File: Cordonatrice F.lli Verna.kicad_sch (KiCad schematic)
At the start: 36 parts, among them J1 Screw_Terminal_3_P5.00mm, J10 Screw_Terminal_2_P5.00mm, J11 Screw_Terminal_2_P5.00mm, J12 Screw_Terminal_4_P5.00mm, J13 Screw_Terminal_2_P5.00mm, J14 Screw_Terminal_2_P5.00mm, J2 Screw_Terminal_3_P5.00mm, J3 Screw_Terminal_3_P5.00mm, J4 Screw_Terminal_3_P5.00mm, J5 Screw_Terminal_3_P5.00mm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

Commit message: sostituzione esp32
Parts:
- removed U1: ESP32-DEVKITC-32UE, ESP32-DEVKITC-32UE:ESPRESSIF_ESP32-DEVKITC-32UE, symbol ESP32-DEVKITC-32UE:ESP32-DEVKITC-32UE
- added U3: ESP32-DEVKITC-32D, ESP32-DEVKITC-32D:MODULE_ESP32-DEVKITC-32D, symbol ESP32-DEVKITC-32D:ESP32-DEVKITC-32D
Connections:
- net +24V: no longer K1.1
- net +3.3V: now also U3.J2-1 (3V3)
- net +5V: now also K1.1, U3.J2-19 (EXT_5V)
- net SCL: now also U3.J3-3 (IO22)
- net SDA: now also U3.J3-6 (IO21)
- net rele_fiaccola: now reaches R1.1
- net rele_fiaccola: now also U3.J3-5 (RXD0)

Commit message: correzione schema corretto
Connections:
- net BT_PAUSE: now also U3.J3-10 (IO5)
- net BT_START: now also U3.J2-13 (IO12)
- net BT_STOP: now also U3.J2-15 (IO13)
- net GND: now also U3.J3-1 (GND3)
- net LIMIT_X_MAX: now also U3.J2-6 (IO35)
- net LIMIT_X_MIN: now also U3.J2-5 (IO34)
- net LIMIT_Y_MAX: now also U3.J2-4 (SENSOR_VN)
- net LIMIT_Y_MIN: now also U3.J2-3 (SENSOR_VP)
- net POT_M1: now also U3.J3-16 (IO15)
- net POT_M2: now also U3.J3-13 (IO4)
- net ENBL_X_MIC.: now reaches U3.J2-10 (IO26)
- net ENBL_X_MIC.: now also U2.3 (A3)
- net DIR_X_MIC.: now reaches U3.J2-11 (IO27)
- net DIR_X_MIC.: now also U2.2 (A2)
- net STEP_X_MIC.: now reaches U3.J2-12 (IO14)
- net STEP_X_MIC.: now also U2.1 (A1)
- net ENBL_Y_MIC.: now reaches U3.J2-7 (IO32)
- net ENBL_Y_MIC.: now also U2.6 (A6)
- net DIR_Y_MIC.: now reaches U3.J2-8 (IO33)
- net DIR_Y_MIC.: now also U2.5 (A5)
- net STEP_Y_MIC.: now reaches U3.J2-9 (IO25)
- net STEP_Y_MIC.: now also U2.4 (A4)
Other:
- moved on the sheet: J14, K1, Q1, R1

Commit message: aggiunta 7824
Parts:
- added C1: 22uF_50V, Capacitor_THT:CP_Radial_D5.0mm_P2.00mm, symbol PCM_SL_Capacitors:22uF_50V
- added C2: 100nF_Ceramic, Capacitor_THT:C_Disc_D5.0mm_W2.5mm_P2.50mm, symbol PCM_SL_Capacitors:100nF_Ceramic
- added U1: LM7812_TO220, Package_TO_SOT_THT:TO-220-3_Vertical, symbol Regulator_Linear:LM7812_TO220
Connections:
- net +24V: now also U1.1 (VI); no longer U4.1 (VI)
- net +5V: now also C1.1, C2.2; no longer C3.2, C6.1
- net GND: now also C1.2, C2.1, U1.2 (GND)
- new net: C3.2, C6.1, U1.3 (VO), U4.1 (VI)
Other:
- moved on the sheet: C3, C4, C5, C6, U4

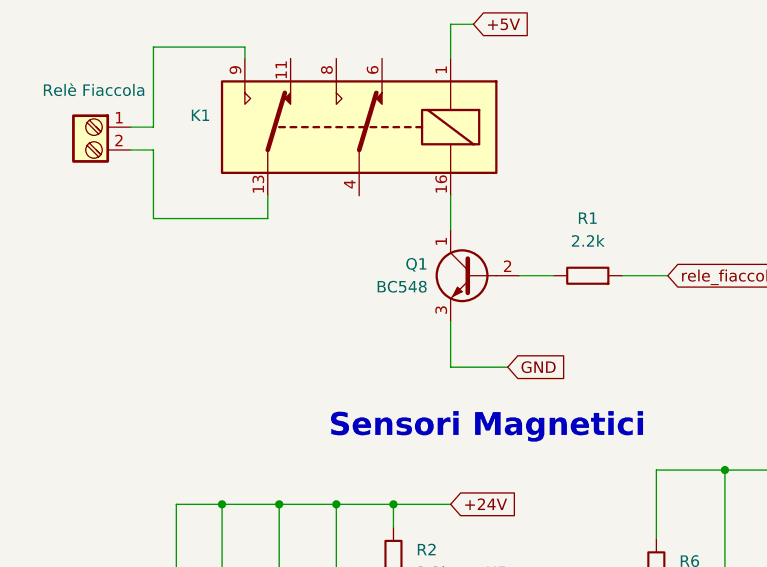
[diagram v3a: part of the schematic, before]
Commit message: aggiunta diodo su transistor
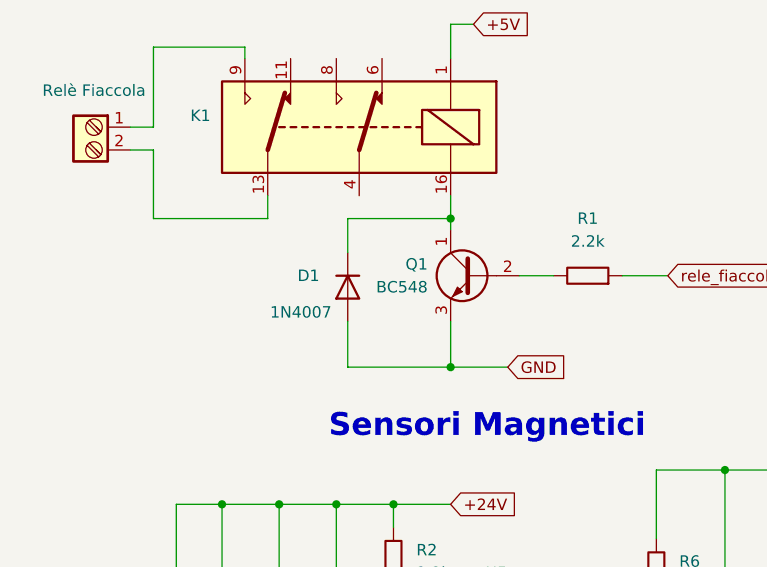
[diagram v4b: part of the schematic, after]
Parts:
- added D1: 1N4007, Diode_THT:D_DO-41_SOD81_P10.16mm_Horizontal, symbol Diode:1N4007
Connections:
- net GND: now also D1.2 (A)
- net at K1.16, Q1.1 (C): now also D1.1 (K)
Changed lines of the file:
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@@
 	)
 	(junction
+		(at 68.58 95.25)
+		(diameter 0)
+		(color 0 0 0 0)
+	)
+	(junction
 		(at 111.76 123.19)
 		(diameter 0)
@@
 	)
 	(junction
+		(at 68.58 111.76)
+		(diameter 0)
+		(color 0 0 0 0)
+	)
+	(junction
 		(at 99.06 154.94)
 		(diameter 0)
@@
 	(wire
 		(pts
+			(xy 57.15 95.25) (xy 68.58 95.25)
+		)
+		(stroke
+			(width 0)
+			(type default)
+		)
+	)
+	(wire
+		(pts
 			(xy 62.23 127) (xy 62.23 129.54)
 		)
@@
 	(wire
 		(pts
+			(xy 57.15 99.06) (xy 57.15 95.25)
+		)
+		(stroke
+			(width 0)
+			(type default)
+		)
+	)
+	(wire
+		(pts
 			(xy 55.88 144.78) (xy 55.88 127)
 		)
@@
 	(wire
 		(pts
+			(xy 68.58 95.25) (xy 68.58 96.52)
+		)
+		(stroke
+			(width 0)
+			(type default)
+		)
+	)
+	(wire
+		(pts
 			(xy 191.77 140.97) (xy 214.63 140.97)
 		)
@@
 	(wire
 		(pts
-			(xy 68.58 92.71) (xy 68.58 96.52)
+			(xy 68.58 92.71) (xy 68.58 95.25)
 		)
 		(stroke
@@
 	(wire
 		(pts
+			(xy 57.15 106.68) (xy 57.15 111.76)
+		)
+		(stroke
+			(width 0)
+			(type default)
+		)
+	)
+	(wire
+		(pts
 			(xy 185.42 96.52) (xy 196.85 96.52)
 		)
@@
 	(wire
 		(pts
+			(xy 57.15 111.76) (xy 68.58 111.76)
+		)
+		(stroke
+			(width 0)
+			(type default)
+		)
+	)
+	(wire
+		(pts
 			(xy 210.82 15.24) (xy 102.87 15.24)
 		)
@@
 					(unit 1)
 				)
+			)
+		)
+	)
+	(symbol
+		(lib_id "Diode:1N4007")
+		(at 57.15 102.87 90)
+		(mirror x)
+		(unit 1)
+		(exclude_from_sim no)
+		(in_bom yes)
+		(on_board yes)
+		(dnp no)
+		(property "Reference" "D1"
+			(at 51.562 101.6 90)
+			(effects
+				(font
+					(size 1.27 1.27)
+				)
+				(justify right)
+			)
+		)
+		(property "Value" "1N4007"
+			(at 48.514 105.664 90)
+			(effects
+				(font
+					(size 1.27 1.27)
+				)
+				(justify right)
+			)
+		)
+		(property "Footprint" "Diode_THT:D_DO-41_SOD81_P10.16mm_Horizontal"
+			(at 61.595 102.87 0)
+			(effects
+				(font
+					(size 1.27 1.27)
+				)
+				(hide yes)
+			)
+		)
+		(property "Datasheet" "http://www.vishay.com/docs/88503/1n4001.pdf"
+			(at 57.15 102.87 0)
+			(effects
+				(font
+					(size 1.27 1.27)
+				)
+				(hide yes)
+			)
+		)
+		(property "Description" "1000V 1A General Purpose Rectifier Diode, DO-41"
+			(at 57.15 102.87 0)
+			(effects
+				(font
+					(size 1.27 1.27)
+				)
+				(hide yes)
+			)
+		)
+		(property "Sim.Device" "D"
+			(at 57.15 102.87 0)
+			(effects
+				(font
+					(size 1.27 1.27)
+				)
+				(hide yes)
+			)
+		)
+		(property "Sim.Pins" "1=K 2=A"
+			(at 57.15 102.87 0)
+			(effects
+				(font
+					(size 1.27 1.27)
+				)
+				(hide yes)
+			)
+		)
+		(pin "2"
+		)
+		(pin "1"
+		)
+		(instances
+			(project ""
+				(path "/38ad800e-5bf8-4838-afd2-3c8a02b76649"
+					(reference "D1")
+					(unit 1)
+				)
